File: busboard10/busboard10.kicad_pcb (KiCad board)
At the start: 2 copper layers, 200 x 25 mm, 18 parts, among them J1 Synth_power_2x5_narrow, J10 Synth_power_2x5_narrow, J11 Synth_power_2x5_narrow, J12 Synth_power_2x5_narrow, J13 Conn_01x03, J2 Synth_power_2x5_narrow, J3 Synth_power_2x5_narrow, J4 Synth_power_2x5_narrow, J5 Synth_power_2x5_narrow, J6 Synth_power_2x5_narrow, J7 Synth_power_2x5_narrow, J8 Synth_power_2x5_narrow, J9 Synth_power_2x5_narrow

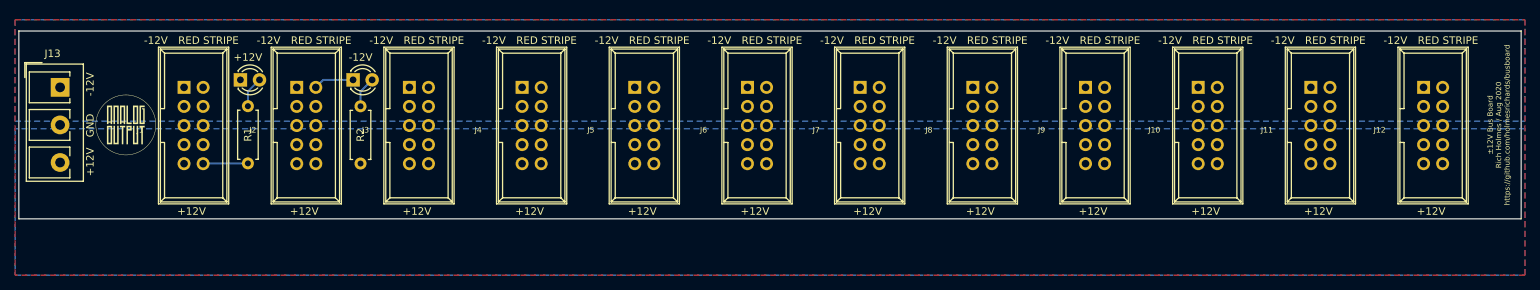
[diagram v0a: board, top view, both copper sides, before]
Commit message: mounting holes
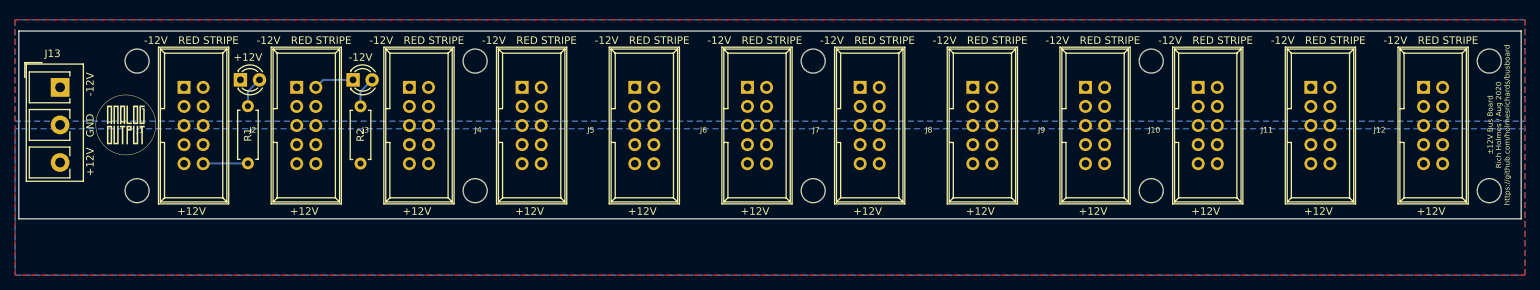
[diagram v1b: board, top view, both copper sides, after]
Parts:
- added REF**: MountingHole_3.2mm_M3, ao_tht:MountingHole_3.2mm_M3, F.Cu at (192.8, 71.2)
- added REF**: MountingHole_3.2mm_M3, ao_tht:MountingHole_3.2mm_M3, F.Cu at (102.8, 54.0)
- added REF**: MountingHole_3.2mm_M3, ao_tht:MountingHole_3.2mm_M3, F.Cu at (102.8, 71.2)
- added REF**: MountingHole_3.2mm_M3, ao_tht:MountingHole_3.2mm_M3, F.Cu at (147.8, 71.2)
- added REF**: MountingHole_3.2mm_M3, ao_tht:MountingHole_3.2mm_M3, F.Cu at (57.8, 71.2)
- added REF**: MountingHole_3.2mm_M3, ao_tht:MountingHole_3.2mm_M3, F.Cu at (237.8, 71.2)
- added REF**: MountingHole_3.2mm_M3, ao_tht:MountingHole_3.2mm_M3, F.Cu at (57.8, 54.0)
- added REF**: MountingHole_3.2mm_M3, ao_tht:MountingHole_3.2mm_M3, F.Cu at (237.8, 54.0)
- added REF**: MountingHole_3.2mm_M3, ao_tht:MountingHole_3.2mm_M3, F.Cu at (192.8, 54.0)
- added REF**: MountingHole_3.2mm_M3, ao_tht:MountingHole_3.2mm_M3, F.Cu at (147.8, 54.0)
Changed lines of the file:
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@@
     (tracks 8)
     (zones 0)
-    (modules 18)
+    (modules 28)
     (nets 6)
   )
@@
     (uvia_drill 0.1)
   )
+  (module ao_tht:MountingHole_3.2mm_M3 locked (layer F.Cu)
+    (at 192.75 71.25)
+    (descr "Mounting Hole 3.2mm, no annular, M3")
+    (tags "mounting hole 3.2mm no annular m3")
+    (attr virtual)
+    (fp_text reference REF** (at 0 -4.2) (layer F.SilkS) hide
+      (effects (font (size 1 1) (thickness 0.15)))
+    )
+    (fp_text value MountingHole_3.2mm_M3 (at 0 4.2) (layer F.Fab)
+      (effects (font (size 1 1) (thickness 0.15)))
+    )
+    (fp_circle (center 0 0) (end 3.45 0) (layer F.CrtYd) (width 0.05))
+    (fp_circle (center 0 0) (end 3.2 0) (layer Cmts.User) (width 0.15))
+    (fp_text user %R (at 0.3 0) (layer F.Fab) hide
+      (effects (font (size 1 1) (thickness 0.15)))
+    )
+    (pad 1 np_thru_hole circle (at 0 0) (size 3.2 3.2) (drill 3.2) (layers *.Cu *.Mask))
+  )
+  (module ao_tht:MountingHole_3.2mm_M3 locked (layer F.Cu)
+    (at 102.75 71.25)
+    (descr "Mounting Hole 3.2mm, no annular, M3")
+    (tags "mounting hole 3.2mm no annular m3")
+    (attr virtual)
+    (fp_text reference REF** (at 0 -4.2) (layer F.SilkS) hide
+      (effects (font (size 1 1) (thickness 0.15)))
+    )
+    (fp_text value MountingHole_3.2mm_M3 (at 0 4.2) (layer F.Fab)
+      (effects (font (size 1 1) (thickness 0.15)))
+    )
+    (fp_circle (center 0 0) (end 3.45 0) (layer F.CrtYd) (width 0.05))
+    (fp_circle (center 0 0) (end 3.2 0) (layer Cmts.User) (width 0.15))
+    (fp_text user %R (at 0.3 0) (layer F.Fab) hide
+      (effects (font (size 1 1) (thickness 0.15)))
+    )
+    (pad 1 np_thru_hole circle (at 0 0) (size 3.2 3.2) (drill 3.2) (layers *.Cu *.Mask))
+  )
+  (module ao_tht:MountingHole_3.2mm_M3 locked (layer F.Cu)
+    (at 147.75 71.25)
+    (descr "Mounting Hole 3.2mm, no annular, M3")
+    (tags "mounting hole 3.2mm no annular m3")
+    (attr virtual)
+    (fp_text reference REF** (at 0 -4.2) (layer F.SilkS) hide
+      (effects (font (size 1 1) (thickness 0.15)))
+    )
+    (fp_text value MountingHole_3.2mm_M3 (at 0 4.2) (layer F.Fab)
+      (effects (font (size 1 1) (thickness 0.15)))
+    )
+    (fp_text user %R (at 0.3 0) (layer F.Fab) hide
+      (effects (font (size 1 1) (thickness 0.15)))
+    )
+    (fp_circle (center 0 0) (end 3.2 0) (layer Cmts.User) (width 0.15))
+    (fp_circle (center 0 0) (end 3.45 0) (layer F.CrtYd) (width 0.05))
+    (pad 1 np_thru_hole circle (at 0 0) (size 3.2 3.2) (drill 3.2) (layers *.Cu *.Mask))
+  )
+  (module ao_tht:MountingHole_3.2mm_M3 locked (layer F.Cu)
+    (at 57.75 71.25)
+    (descr "Mounting Hole 3.2mm, no annular, M3")
+    (tags "mounting hole 3.2mm no annular m3")
+    (attr virtual)
+    (fp_text reference REF** (at 0 -4.2) (layer F.SilkS) hide
+      (effects (font (size 1 1) (thickness 0.15)))
+    )
+    (fp_text value MountingHole_3.2mm_M3 (at 0 4.2) (layer F.Fab)
+      (effects (font (size 1 1) (thickness 0.15)))
+    )
+    (fp_circle (center 0 0) (end 3.45 0) (layer F.CrtYd) (width 0.05))
+    (fp_circle (center 0 0) (end 3.2 0) (layer Cmts.User) (width 0.15))
+    (fp_text user %R (at 0.3 0) (layer F.Fab) hide
+      (effects (font (size 1 1) (thickness 0.15)))
+    )
+    (pad 1 np_thru_hole circle (at 0 0) (size 3.2 3.2) (drill 3.2) (layers *.Cu *.Mask))
+  )
+  (module ao_tht:MountingHole_3.2mm_M3 locked (layer F.Cu)
+    (at 237.75 71.25)
+    (descr "Mounting Hole 3.2mm, no annular, M3")
+    (tags "mounting hole 3.2mm no annular m3")
+    (attr virtual)
+    (fp_text reference REF** (at 0 -4.2) (layer F.SilkS) hide
+      (effects (font (size 1 1) (thickness 0.15)))
+    )
+    (fp_text value MountingHole_3.2mm_M3 (at 0 4.2) (layer F.Fab)
+      (effects (font (size 1 1) (thickness 0.15)))
+    )
+    (fp_text user %R (at 0.3 0) (layer F.Fab) hide
+      (effects (font (size 1 1) (thickness 0.15)))
+    )
+    (fp_circle (center 0 0) (end 3.2 0) (layer Cmts.User) (width 0.15))
+    (fp_circle (center 0 0) (end 3.45 0) (layer F.CrtYd) (width 0.05))
+    (pad 1 np_thru_hole circle (at 0 0) (size 3.2 3.2) (drill 3.2) (layers *.Cu *.Mask))
+  )
+  (module ao_tht:MountingHole_3.2mm_M3 locked (layer F.Cu)
+    (at 57.75 54)
+    (descr "Mounting Hole 3.2mm, no annular, M3")
+    (tags "mounting hole 3.2mm no annular m3")
+    (attr virtual)
+    (fp_text reference REF** (at 0 -4.2) (layer F.SilkS) hide
+      (effects (font (size 1 1) (thickness 0.15)))
+    )
+    (fp_text value MountingHole_3.2mm_M3 (at 0 4.2) (layer F.Fab)
+      (effects (font (size 1 1) (thickness 0.15)))
+    )
+    (fp_text user %R (at 0.3 0) (layer F.Fab) hide
+      (effects (font (size 1 1) (thickness 0.15)))
+    )
+    (fp_circle (center 0 0) (end 3.2 0) (layer Cmts.User) (width 0.15))
+    (fp_circle (center 0 0) (end 3.45 0) (layer F.CrtYd) (width 0.05))
+    (pad 1 np_thru_hole circle (at 0 0) (size 3.2 3.2) (drill 3.2) (layers *.Cu *.Mask))
+  )
+  (module ao_tht:MountingHole_3.2mm_M3 locked (layer F.Cu)
+    (at 237.75 54)
+    (descr "Mounting Hole 3.2mm, no annular, M3")
+    (tags "mounting hole 3.2mm no annular m3")
+    (attr virtual)
+    (fp_text reference REF** (at 0 -4.2) (layer F.SilkS) hide
+      (effects (font (size 1 1) (thickness 0.15)))
+    )
+    (fp_text value MountingHole_3.2mm_M3 (at 0 4.2) (layer F.Fab)
+      (effects (font (size 1 1) (thickness 0.15)))
+    )
+    (fp_circle (center 0 0) (end 3.45 0) (layer F.CrtYd) (width 0.05))
+    (fp_circle (center 0 0) (end 3.2 0) (layer Cmts.User) (width 0.15))
+    (fp_text user %R (at 0.3 0) (layer F.Fab) hide
+      (effects (font (size 1 1) (thickness 0.15)))
+    )
+    (pad 1 np_thru_hole circle (at 0 0) (size 3.2 3.2) (drill 3.2) (layers *.Cu *.Mask))
+  )
+  (module ao_tht:MountingHole_3.2mm_M3 locked (layer F.Cu)
+    (at 192.75 54)
+    (descr "Mounting Hole 3.2mm, no annular, M3")
+    (tags "mounting hole 3.2mm no annular m3")
+    (attr virtual)
+    (fp_text reference REF** (at 0 -4.2) (layer F.SilkS) hide
+      (effects (font (size 1 1) (thickness 0.15)))
+    )
+    (fp_text value MountingHole_3.2mm_M3 (at 0 4.2) (layer F.Fab)
+      (effects (font (size 1 1) (thickness 0.15)))
+    )
+    (fp_text user %R (at 0.3 0) (layer F.Fab) hide
+      (effects (font (size 1 1) (thickness 0.15)))
+    )
+    (fp_circle (center 0 0) (end 3.2 0) (layer Cmts.User) (width 0.15))
+    (fp_circle (center 0 0) (end 3.45 0) (layer F.CrtYd) (width 0.05))
+    (pad 1 np_thru_hole circle (at 0 0) (size 3.2 3.2) (drill 3.2) (layers *.Cu *.Mask))
+  )
+  (module ao_tht:MountingHole_3.2mm_M3 locked (layer F.Cu)
+    (at 147.75 54)
+    (descr "Mounting Hole 3.2mm, no annular, M3")
+    (tags "mounting hole 3.2mm no annular m3")
+    (attr virtual)
+    (fp_text reference REF** (at 0 -4.2) (layer F.SilkS) hide
+      (effects (font (size 1 1) (thickness 0.15)))
+    )
+    (fp_text value MountingHole_3.2mm_M3 (at 0 4.2) (layer F.Fab)
+      (effects (font (size 1 1) (thickness 0.15)))
+    )
+    (fp_circle (center 0 0) (end 3.45 0) (layer F.CrtYd) (width 0.05))
+    (fp_circle (center 0 0) (end 3.2 0) (layer Cmts.User) (width 0.15))
+    (fp_text user %R (at 0.3 0) (layer F.Fab) hide
+      (effects (font (size 1 1) (thickness 0.15)))
+    )
+    (pad 1 np_thru_hole circle (at 0 0) (size 3.2 3.2) (drill 3.2) (layers *.Cu *.Mask))
+  )
+  (module ao_tht:MountingHole_3.2mm_M3 locked (layer F.Cu)
+    (at 102.75 54)
+    (descr "Mounting Hole 3.2mm, no annular, M3")
+    (tags "mounting hole 3.2mm no annular m3")
+    (attr virtual)
+    (fp_text reference REF** (at 0 -4.2) (layer F.SilkS) hide
+      (effects (font (size 1 1) (thickness 0.15)))
+    )
+    (fp_text value MountingHole_3.2mm_M3 (at 0 4.2) (layer F.Fab)
+      (effects (font (size 1 1) (thickness 0.15)))
+    )
+    (fp_text user %R (at 0.3 0) (layer F.Fab) hide
+      (effects (font (size 1 1) (thickness 0.15)))
+    )
+    (fp_circle (center 0 0) (end 3.2 0) (layer Cmts.User) (width 0.15))
+    (fp_circle (center 0 0) (end 3.45 0) (layer F.CrtYd) (width 0.05))
+    (pad 1 np_thru_hole circle (at 0 0) (size 3.2 3.2) (drill 3.2) (layers *.Cu *.Mask))
+  )
   (module busboard10:analogoutput_8mm locked (layer F.Cu)
